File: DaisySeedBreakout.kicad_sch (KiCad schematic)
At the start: 24 parts, among them J24 Conn_01x02, J25 Conn_01x02, J26 Conn_02x04, J30 Conn_01x02, J31 Conn_02x04, J32 Conn_01x02, J33 Conn_01x02, J34 Conn_01x02, J35 Conn_01x02, J6 Conn_01x02

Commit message: Minor modifications
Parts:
- added C9: 0.1uF, Capacitor_SMD:C_0402_1005Metric, symbol Device:C
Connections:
- net GND: now also C9.2
- net at A1.21 (3V3_A): now also C9.1
- net Analog_out_conn/AO_Conn renamed AO0
- net Analog_out_conn1/AO_Conn renamed AO1
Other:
- moved on the sheet: C3

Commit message: Placeholder for speaker driver
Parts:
- added C10, C25: 220pF, Capacitor_SMD:C_0402_1005Metric, symbol Device:C
- added FB1, FB2: BLM21PG221SN1D, digikey-footprints:0805, symbol dk_Ferrite-Beads-and-Chips:BLM21PG221SN1D
- added U2: PAM8320RDR, SO-16EP_3P9X9P9_DIO, symbol 2023-10-01_02-32-05:PAM8320RDR
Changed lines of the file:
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@@
   )
   (text "Accelerometer/Magnometer/Gyroscope/Temperature Sensor"
-    (at 458.47 27.94 0)
+    (at 640.08 21.59 0)
     (effects (font (size 5.27 5.27)) (justify left bottom))
   )
@@
     )
   )
+  (symbol (lib_id "Device:C") (at 128.27 152.4 0) (unit 1)
+    (in_bom yes) (on_board yes) (dnp no) (fields_autoplaced)
+    (property "Reference" "C10" (at 132.08 151.13 0)
+      (effects (font (size 1.27 1.27)) (justify left))
+    )
+    (property "Value" "220pF" (at 132.08 153.67 0)
+      (effects (font (size 1.27 1.27)) (justify left))
+    )
+    (property "Footprint" "Capacitor_SMD:C_0402_1005Metric" (at 129.2352 156.21 0)
+      (effects (font (size 1.27 1.27)) hide)
+    )
+    (property "Datasheet" "~" (at 128.27 152.4 0)
+      (effects (font (size 1.27 1.27)) hide)
+    )
+    (pin "1")
+    (pin "2")
+    (instances
+      (project "DaisySeedBreakout"
+        (path "/a83c9f4b-f61b-47d4-b39d-4636bff6eb0e"
+          (reference "C10") (unit 1)
+        )
+        (path "/a83c9f4b-f61b-47d4-b39d-4636bff6eb0e/d5f93f74-350a-43ef-bdfb-299723239788"
+          (reference "C24") (unit 1)
+        )
+      )
+    )
+  )
   (symbol (lib_id "4ms_Connector:Conn_02x04") (at 98.552 198.247 0) (unit 1)
     (in_bom yes) (on_board yes) (dnp no) (fields_autoplaced)
@@
     )
   )
+  (symbol (lib_id "dk_Ferrite-Beads-and-Chips:BLM21PG221SN1D") (at 111.76 148.59 0) (unit 1)
+    (in_bom yes) (on_board yes) (dnp no) (fields_autoplaced)
+    (property "Reference" "FB1" (at 111.76 140.97 0)
+      (effects (font (size 1.524 1.524)))
+    )
+    (property "Value" "BLM21PG221SN1D" (at 111.76 143.51 0)
+      (effects (font (size 1.524 1.524)))
+    )
+    (property "Footprint" "digikey-footprints:0805" (at 116.84 143.51 0)
+      (effects (font (size 1.524 1.524)) (justify left) hide)
+    )
+    (property "Datasheet" "https://www.murata.com/en-us/products/en-us/products/productdata/8796738977822/ENFA0005.pdf" (at 116.84 140.97 0)
+      (effects (font (size 1.524 1.524)) (justify left) hide)
+    )
+    (property "Digi-Key_PN" "490-1054-1-ND" (at 116.84 138.43 0)
+      (effects (font (size 1.524 1.524)) (justify left) hide)
+    )
+    (property "MPN" "BLM21PG221SN1D" (at 116.84 135.89 0)
+      (effects (font (size 1.524 1.524)) (justify left) hide)
+    )
+    (property "Category" "Filters" (at 116.84 133.35 0)
+      (effects (font (size 1.524 1.524)) (justify left) hide)
+    )
+    (property "Family" "Ferrite Beads and Chips" (at 116.84 130.81 0)
+      (effects (font (size 1.524 1.524)) (justify left) hide)
+    )
+    (property "DK_Datasheet_Link" "https://www.murata.com/en-us/products/en-us/products/productdata/8796738977822/ENFA0005.pdf" (at 116.84 128.27 0)
+      (effects (font (size 1.524 1.524)) (justify left) hide)
+    )
+    (property "DK_Detail_Page" "/product-detail/en/murata-electronics-north-america/BLM21PG221SN1D/490-1054-1-ND/574418" (at 116.84 125.73 0)
+      (effects (font (size 1.524 1.524)) (justify left) hide)
+    )
+    (property "Description" "FERRITE BEAD 220 OHM 0805 1LN" (at 116.84 123.19 0)
+      (effects (font (size 1.524 1.524)) (justify left) hide)
+    )
+    (property "Manufacturer" "Murata Electronics North America" (at 116.84 120.65 0)
+      (effects (font (size 1.524 1.524)) (justify left) hide)
+    )
+    (property "Status" "Active" (at 116.84 118.11 0)
+      (effects (font (size 1.524 1.524)) (justify left) hide)
+    )
+    (pin "1")
+    (pin "2")
+    (instances
+      (project "DaisySeedBreakout"
+        (path "/a83c9f4b-f61b-47d4-b39d-4636bff6eb0e"
+          (reference "FB1") (unit 1)
+        )
+      )
+    )
+  )
   (symbol (lib_id "power:+3.3V") (at 238.76 113.03 0) (unit 1)
     (in_bom yes) (on_board yes) (dnp no) (fields_autoplaced)
@@
     )
   )
+  (symbol (lib_id "2023-10-01_02-32-05:PAM8320RDR") (at 46.99 143.51 0) (unit 1)
+    (in_bom yes) (on_board yes) (dnp no) (fields_autoplaced)
+    (property "Reference" "U2" (at 69.85 133.35 0)
+      (effects (font (size 1.524 1.524)))
+    )
+    (property "Value" "PAM8320RDR" (at 69.85 135.89 0)
+      (effects (font (size 1.524 1.524)))
+    )
+    (property "Footprint" "SO-16EP_3P9X9P9_DIO" (at 46.99 143.51 0)
+      (effects (font (size 1.27 1.27) italic) hide)
+    )
+    (property "Datasheet" "PAM8320RDR" (at 46.99 143.51 0)
+      (effects (font (size 1.27 1.27) italic) hide)
+    )
+    (pin "1")
+    (pin "10")
+    (pin "11")
+    (pin "12")
+    (pin "13")
+    (pin "14")
+    (pin "15")
+    (pin "16")
+    (pin "17")
+    (pin "2")
+    (pin "3")
+    (pin "4")
+    (pin "5")
+    (pin "6")
+    (pin "7")
+    (pin "8")
+    (pin "9")
+    (instances
+      (project "DaisySeedBreakout"
+        (path "/a83c9f4b-f61b-47d4-b39d-4636bff6eb0e"
+          (reference "U2") (unit 1)
+        )
+      )
+    )
+  )
   (symbol (lib_id "power:+3.3V") (at 257.81 75.565 0) (unit 1)
     (in_bom yes) (on_board yes) (dnp no) (fields_autoplaced)
@@
         (path "/a83c9f4b-f61b-47d4-b39d-4636bff6eb0e"
           (reference "R50") (unit 1)
+        )
+      )
+    )
+  )
+  (symbol (lib_id "Device:C") (at 128.27 165.1 0) (unit 1)
+    (in_bom yes) (on_board yes) (dnp no) (fields_autoplaced)
+    (property "Reference" "C25" (at 132.08 163.83 0)
+      (effects (font (size 1.27 1.27)) (justify left))
+    )
+    (property "Value" "220pF" (at 132.08 166.37 0)
+      (effects (font (size 1.27 1.27)) (justify left))
+    )
+    (property "Footprint" "Capacitor_SMD:C_0402_1005Metric" (at 129.2352 168.91 0)
+      (effects (font (size 1.27 1.27)) hide)
+    )
+    (property "Datasheet" "~" (at 128.27 165.1 0)
+      (effects (font (size 1.27 1.27)) hide)
+    )
+    (pin "1")
+    (pin "2")
+    (instances
+      (project "DaisySeedBreakout"
+        (path "/a83c9f4b-f61b-47d4-b39d-4636bff6eb0e"
+          (reference "C25") (unit 1)
+        )
+        (path "/a83c9f4b-f61b-47d4-b39d-4636bff6eb0e/d5f93f74-350a-43ef-bdfb-299723239788"
+          (reference "C24") (unit 1)
         )
       )
@@
         )
       )
+    )
+  )
+  (symbol (lib_id "dk_Ferrite-Beads-and-Chips:BLM21PG221SN1D") (at 111.76 161.29 0) (unit 1)
+    (in_bom yes) (on_board yes) (dnp no) (fields_autoplaced)
+    (property "Reference" "FB2" (at 111.76 153.67 0)
+      (effects (font (size 1.524 1.524)))
+    )
+    (property "Value" "BLM21PG221SN1D" (at 111.76 156.21 0)
+      (effects (font (size 1.524 1.524)))
+    )
+    (property "Footprint" "digikey-footprints:0805" (at 116.84 156.21 0)
+      (effects (font (size 1.524 1.524)) (justify left) hide)
+    )
+    (property "Datasheet" "https://www.murata.com/en-us/products/en-us/products/productdata/8796738977822/ENFA0005.pdf" (at 116.84 153.67 0)
+      (effects (font (size 1.524 1.524)) (justify left) hide)
+    )
+    (property "Digi-Key_PN" "490-1054-1-ND" (at 116.84 151.13 0)
+      (effects (font (size 1.524 1.524)) (justify left) hide)
+    )
+    (property "MPN" "BLM21PG221SN1D" (at 116.84 148.59 0)
+      (effects (font (size 1.524 1.524)) (justify left) hide)
+    )
+    (property "Category" "Filters" (at 116.84 146.05 0)
+      (effects (font (size 1.524 1.524)) (justify left) hide)
+    )
+    (property "Family" "Ferrite Beads and Chips" (at 116.84 143.51 0)
+      (effects (font (size 1.524 1.524)) (justify left) hide)
+    )
+    (property "DK_Datasheet_Link" "https://www.murata.com/en-us/products/en-us/products/productdata/8796738977822/ENFA0005.pdf" (at 116.84 140.97 0)
+      (effects (font (size 1.524 1.524)) (justify left) hide)
+    )
+    (property "DK_Detail_Page" "/product-detail/en/murata-electronics-north-america/BLM21PG221SN1D/490-1054-1-ND/574418" (at 116.84 138.43 0)
+      (effects (font (size 1.524 1.524)) (justify left) hide)
+    )
+    (property "Description" "FERRITE BEAD 220 OHM 0805 1LN" (at 116.84 135.89 0)
+      (effects (font (size 1.524 1.524)) (justify left) hide)
+    )
+    (property "Manufacturer" "Murata Electronics North America" (at 116.84 133.35 0)
+      (effects (font (size 1.524 1.524)) (justify left) hide)
+    )
+    (property "Status" "Active" (at 116.84 130.81 0)
+      (effects (font (size 1.524 1.524)) (justify left) hide)
+    )
+    (pin "1")
+    (pin "2")
+    (instances
+      (project "DaisySeedBreakout"
+        (path "/a83c9f4b-f61b-47d4-b39d-4636bff6eb0e"
+          (reference "FB2") (unit 1)
+        )
+      )

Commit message: add input fuse holder, TVS, reverse diode protection, placeholder 5V LDO
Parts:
- removed C10, C25: 220pF, Capacitor_SMD:C_0402_1005Metric, symbol Device:C
- removed FB1, FB2: BLM21PG221SN1D, digikey-footprints:0805, symbol dk_Ferrite-Beads-and-Chips:BLM21PG221SN1D
- removed U2: PAM8320RDR, SO-16EP_3P9X9P9_DIO, symbol 2023-10-01_02-32-05:PAM8320RDR
- added C57, C58, C59: 0.1uF, Capacitor_SMD:C_0402_1005Metric, symbol Device:C
- added C60: 47uF, Capacitor_SMD:C_0805_2012Metric, symbol Device:C
- added CR1: DFLT15A-7, ZDO_POWERDI123_DIO, symbol 2023-10-02_00-55-35:DFLT15A-7
- added J2: Conn_01x02, Connector_PinHeader_2.54mm:PinHeader_1x02_P2.54mm_Vertical, symbol 4ms_Connector:Conn_01x02
- added J5: ~, Ultralibrarian:BladeFuseHolder, symbol Ultralibrarian_modified_symbols:BladeFuseHolder
- added R56: RSX501LAM20TR, DIO_RB050LAM_ROM, symbol 2023-10-01_23-34-18:RSX501LAM20TR
- added U7: LM317MDCYR, DCY4, symbol 2023-10-02_00-54-17:LM317MDCYR
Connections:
- net +9V is gone; now on net +12V: A1.39 (VIN), C6.1
- net GND: now also J34.2 (Pin_2), J35.2 (Pin_2), C57.2, C58.2, C59.2, C60.2, CR1.2
- net +12V: now reaches J34.1 (Pin_1)
- net +12V: now also C59.1, C60.1, R56.2, U7.2 (INPUT)
- net at J35.1 (Pin_1): now also J5.1 (IN1), J5.2 (IN2)
- new net: C57.1, C58.1, CR1.1, J5.3 (OUT1), J5.4 (OUT2), R56.1
- new net +5V: U7.1 (OUTPUT), U7.3 (OUTPUT)
- new net ClassD_20W_Amp/OUT_N: J2.2 (Pin_2)
- new net ClassD_20W_Amp/OUT_P: J2.1 (Pin_1)
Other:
- removed sheet GPIO_Conn10
- added sheet ClassD_20W_Amp (ClassD_20W_Amp.kicad_sch)
- note added: "Eurorack +-10V compatibility? Add op amp that can be configured for either?"
- moved on the sheet: J30, J34, J35

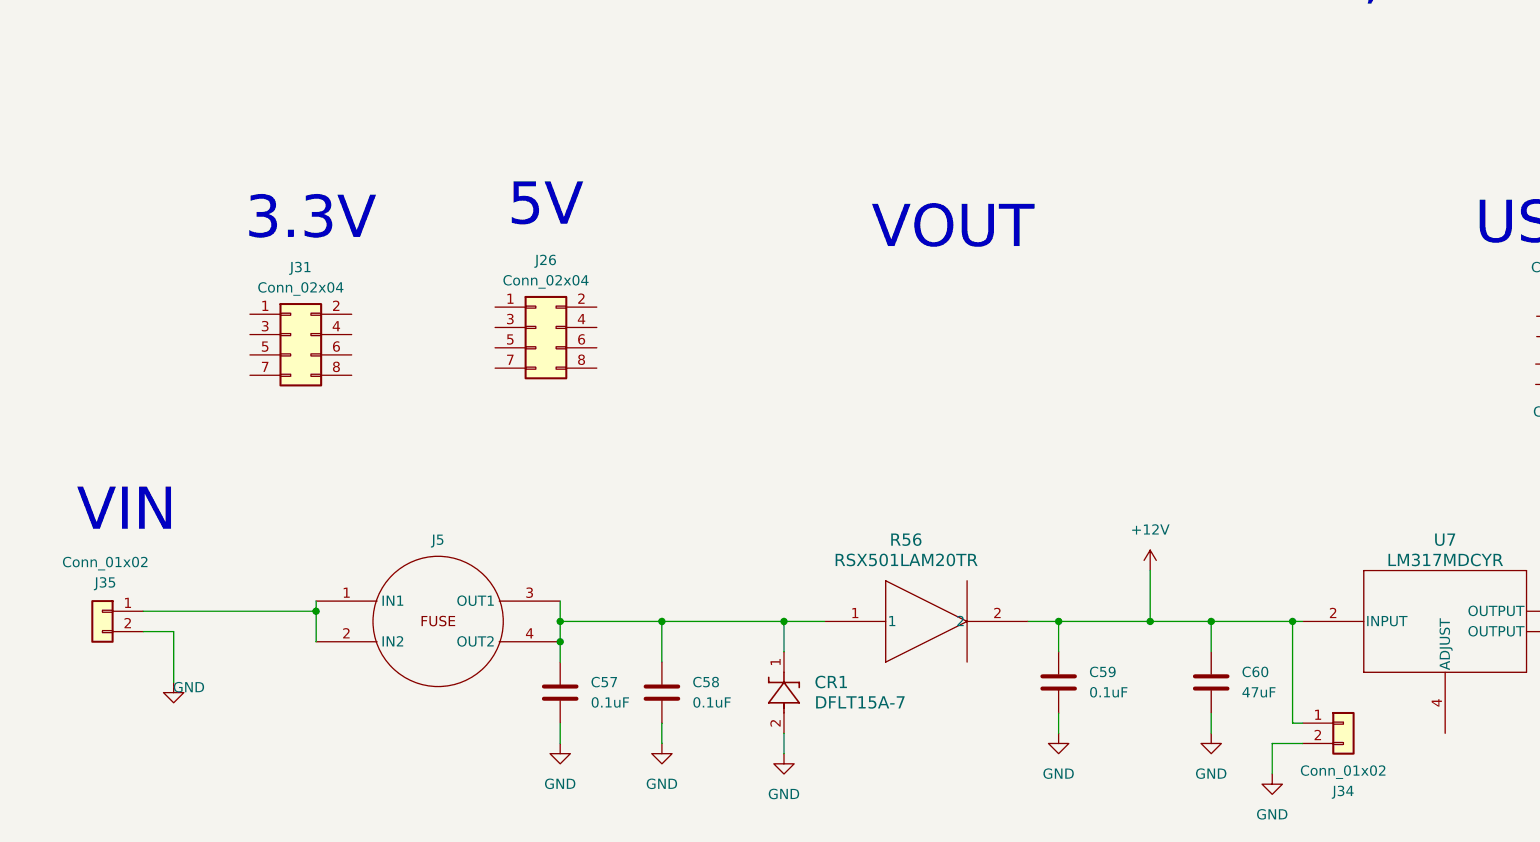
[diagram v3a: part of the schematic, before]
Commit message: add input fuse holder, TVS, reverse diode protection, placeholder 5V LDO
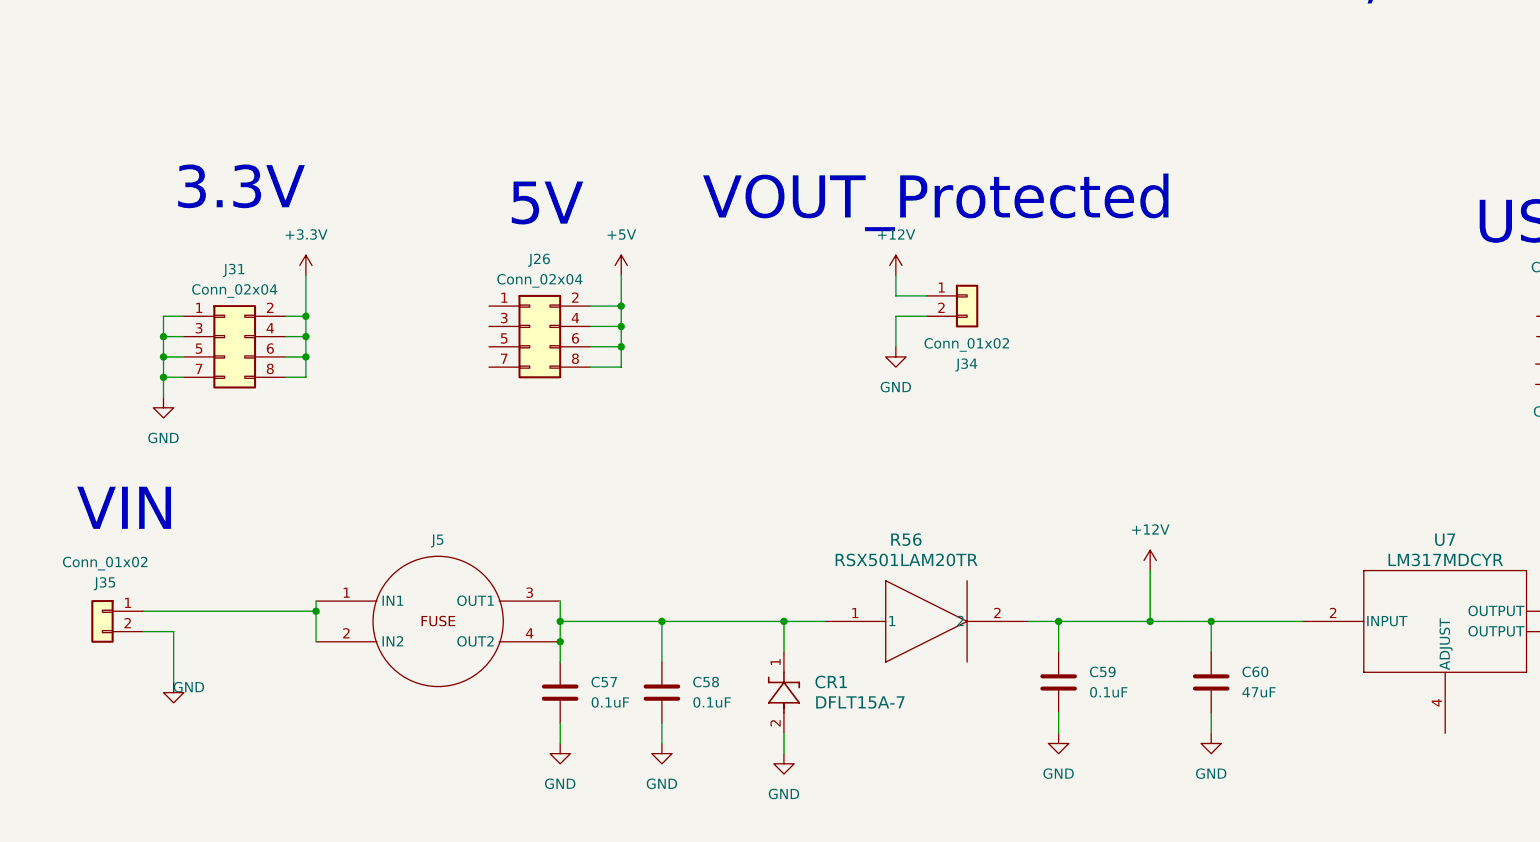
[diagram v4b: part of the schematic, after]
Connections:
- net +3.3V: now also J31.2 (Pin_2), J31.4 (Pin_4), J31.6 (Pin_6), J31.8 (Pin_8)
- net +5V: now also J26.2 (Pin_2), J26.4 (Pin_4), J26.6 (Pin_6), J26.8 (Pin_8)
- net GND: now also J31.1 (Pin_1), J31.3 (Pin_3), J31.5 (Pin_5), J31.7 (Pin_7)
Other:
- note added: "VOUT_Protected"
- note removed: "VOUT"
- moved on the sheet: J26, J31, J34

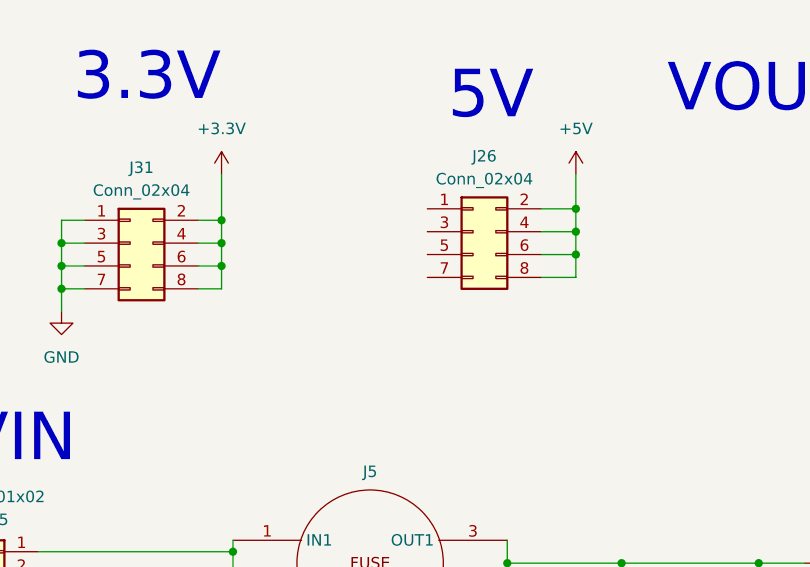
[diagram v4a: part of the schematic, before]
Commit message: add input fuse holder, TVS, reverse diode protection, placeholder 5V LDO
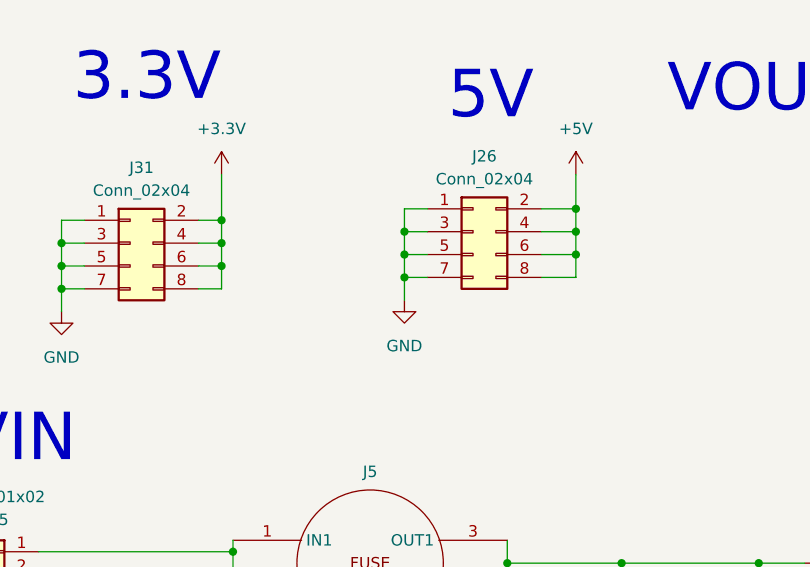
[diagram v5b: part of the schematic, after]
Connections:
- net GND: now also J26.1 (Pin_1), J26.3 (Pin_3), J26.5 (Pin_5), J26.7 (Pin_7)
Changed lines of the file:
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@@
   (junction (at 190.5 134.62) (diameter 0) (color 0 0 0 0)
   )
+  (junction (at 90.17 200.66) (diameter 0) (color 0 0 0 0)
+  )
   (junction (at 109.22 195.58) (diameter 0) (color 0 0 0 0)
   )
+  (junction (at 90.17 203.2) (diameter 0) (color 0 0 0 0)
+  )
   (junction (at 250.19 90.17) (diameter 0) (color 0 0 0 0)
   )
@@
   (junction (at 109.22 198.12) (diameter 0) (color 0 0 0 0)
   )
+  (junction (at 90.17 198.12) (diameter 0) (color 0 0 0 0)
+  )
   (junction (at 114.3 234.95) (diameter 0) (color 0 0 0 0)
   )
@@
     (stroke (width 0) (type default))
   )
+  (wire (pts (xy 90.17 203.2) (xy 92.71 203.2))
+    (stroke (width 0) (type default))
+  )
   (wire (pts (xy 101.6 234.95) (xy 101.6 237.49))
     (stroke (width 0) (type default))
@@
     (stroke (width 0) (type default))
   )
+  (wire (pts (xy 90.17 200.66) (xy 92.71 200.66))
+    (stroke (width 0) (type default))
+  )
   (wire (pts (xy 186.69 53.975) (xy 190.5 53.975))
     (stroke (width 0) (type default))
@@
     (stroke (width 0) (type default))
   )
+  (wire (pts (xy 90.17 200.66) (xy 90.17 203.2))
+    (stroke (width 0) (type default))
+  )
   (wire (pts (xy 139.7 80.01) (xy 167.64 80.01))
     (stroke (width 0) (type default))
@@
     (stroke (width 0) (type default))
   )
+  (wire (pts (xy 90.17 203.2) (xy 90.17 205.74))
+    (stroke (width 0) (type default))
+  )
+  (wire (pts (xy 90.17 198.12) (xy 92.71 198.12))
+    (stroke (width 0) (type default))
+  )
   (wire (pts (xy 381 43.18) (xy 388.62 43.18))
     (stroke (width 0) (type default))
@@
     (stroke (width 0) (type default))
   )
+  (wire (pts (xy 90.17 195.58) (xy 90.17 198.12))
+    (stroke (width 0) (type default))
+  )
   (wire (pts (xy 353.06 123.19) (xy 365.76 123.19))
     (stroke (width 0) (type default))
@@
     (stroke (width 0) (type default))
   )
+  (wire (pts (xy 92.71 195.58) (xy 90.17 195.58))
+    (stroke (width 0) (type default))
+  )
   (wire (pts (xy 262.89 87.63) (xy 257.81 87.63))
     (stroke (width 0) (type default))
   )
   (wire (pts (xy 157.48 107.95) (xy 157.48 114.3))
+    (stroke (width 0) (type default))
+  )
+  (wire (pts (xy 90.17 198.12) (xy 90.17 200.66))
     (stroke (width 0) (type default))
   )
@@
         )
       )
+    )
+  )
+  (symbol (lib_id "power:GND") (at 90.17 205.74 0) (unit 1)
+    (in_bom yes) (on_board yes) (dnp no) (fields_autoplaced)
+    (property "Reference" "#PWR0153" (at 90.17 212.09 0)
+      (effects (font (size 1.27 1.27)) hide)
+    )
+    (property "Value" "GND" (at 90.17 210.82 0)
+      (effects (font (size 1.27 1.27)))
+    )
+    (property "Footprint" "" (at 90.17 205.74 0)
+      (effects (font (size 1.27 1.27)) hide)
+    )
+    (property "Datasheet" "" (at 90.17 205.74 0)
+      (effects (font (size 1.27 1.27)) hide)
+    )
+    (pin "1")
+    (instances
+      (project "DaisySeedBreakout"
+        (path "/a83c9f4b-f61b-47d4-b39d-4636bff6eb0e"
+          (reference "#PWR0153") (unit 1)
+        )
+      )
